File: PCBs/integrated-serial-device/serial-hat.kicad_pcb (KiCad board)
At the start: 2 copper layers, 193 x 113 mm, 30 parts, among them CN1 Modem port, CN2 Modem out 3, CN3 Printer port, J1 Rpi headers, J3 Conn_01x02_Pin, K1 Quicktake, K2 ImageWriter, SW1 Modem To Proxy, SW2 Modem to Quicktake, SW3 Modem out 3, SW5 Printer to Proxy, SW6 Printer to ImageWriter, SW7 SW_SPST, SW8 SW_Slide_DPDT SHOU HAN MSK-22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, U1 MAX3232, U2 PC817C-S

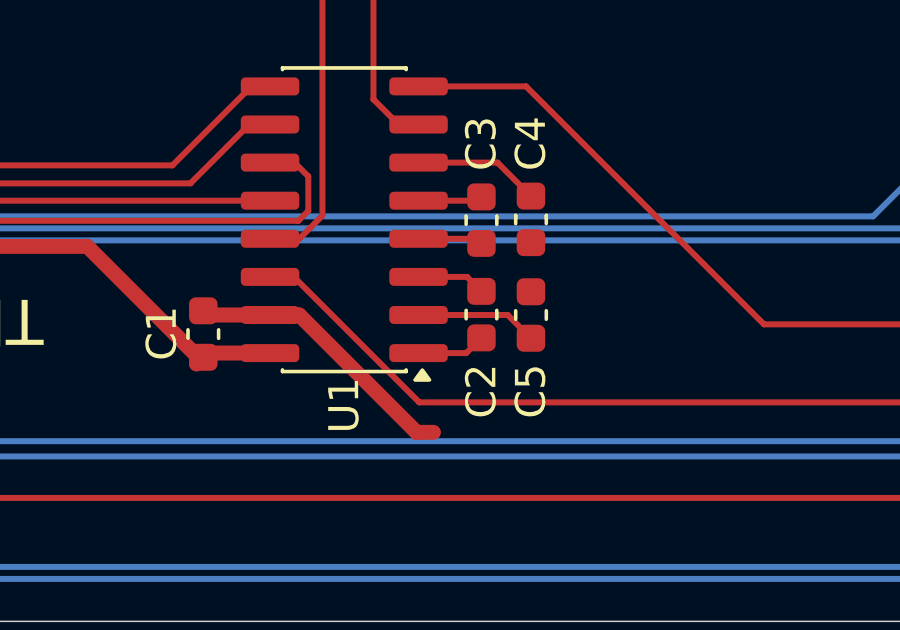
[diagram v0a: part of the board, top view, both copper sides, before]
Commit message: Add teardrops
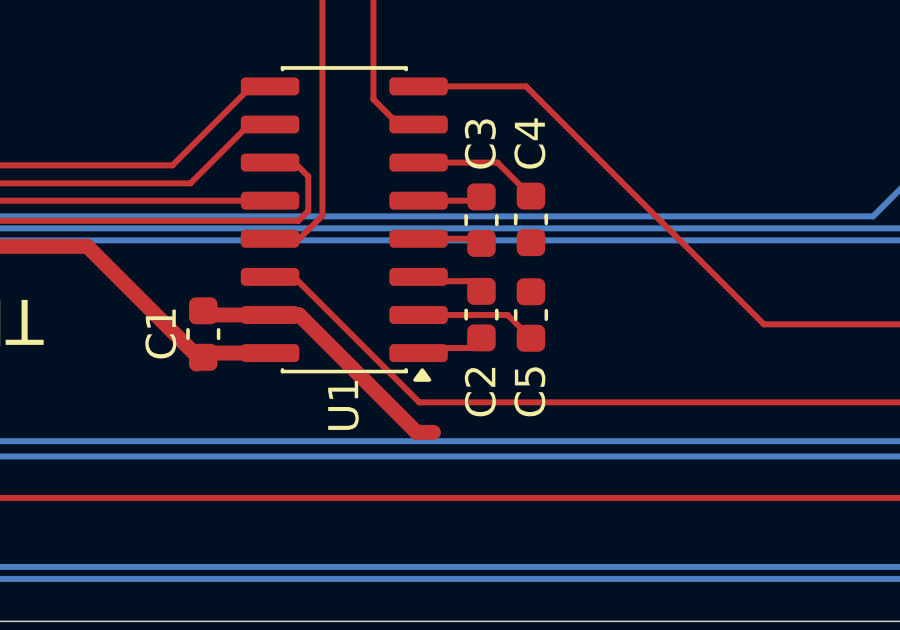
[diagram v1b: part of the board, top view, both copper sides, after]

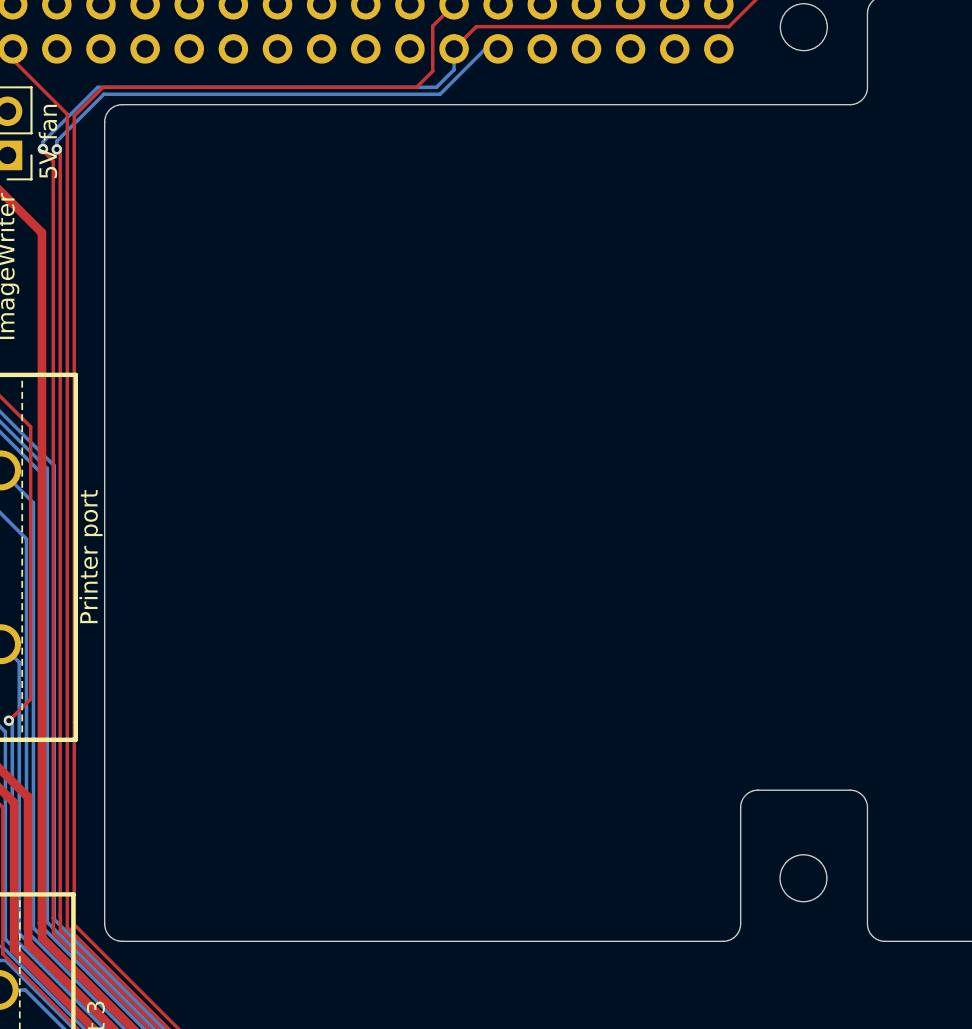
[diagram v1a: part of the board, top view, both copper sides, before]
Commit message: Add fan mounting holes
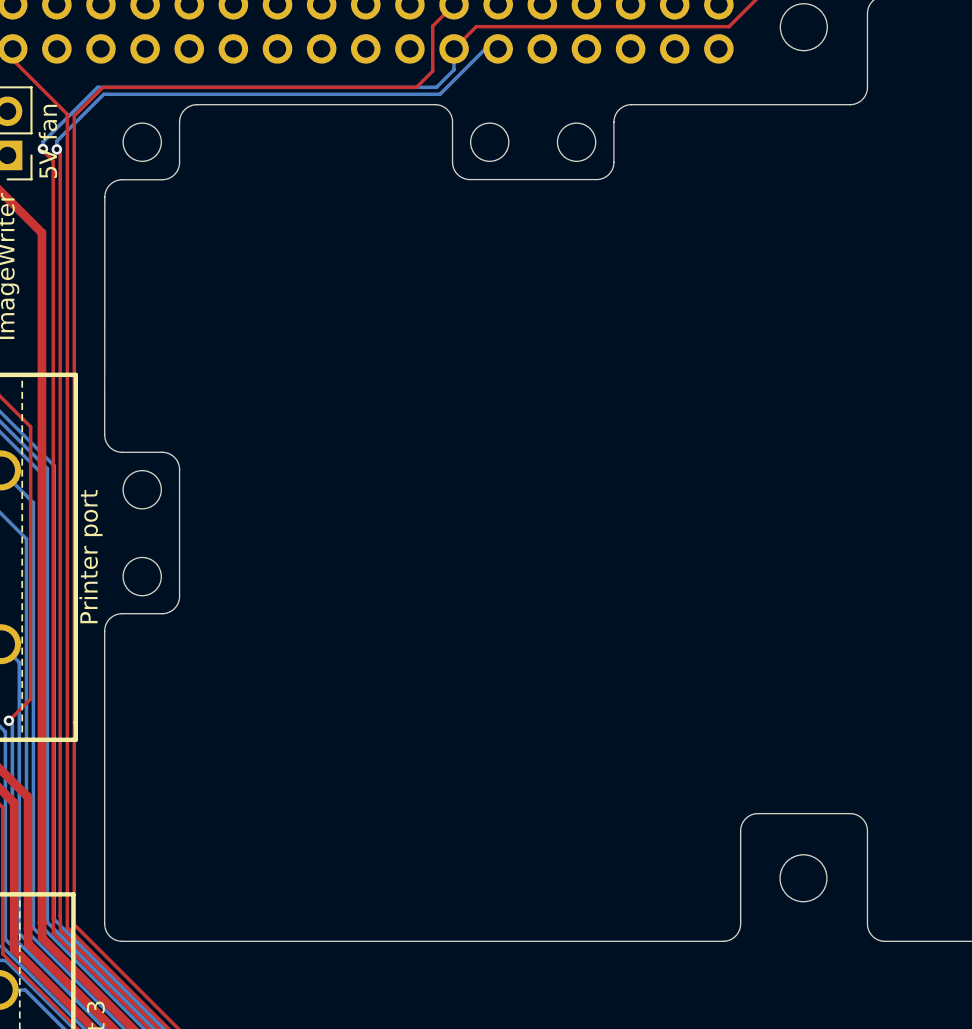
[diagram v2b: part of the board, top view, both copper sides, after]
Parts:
- added ?: , , F.Cu at (76.7, 73.6)
- added ?: , , F.Cu at (76.7, 68.6)
- added REF**: MountingHole_2.2mm_M2_DIN965, MountingHole:MountingHole_2.2mm_M2_DIN965, F.Cu at (76.7, 48.6)
- added REF**: MountingHole_2.2mm_M2_DIN965, MountingHole:MountingHole_2.2mm_M2_DIN965, F.Cu at (101.7, 48.6)
- added REF**: MountingHole_2.2mm_M2_DIN965, MountingHole:MountingHole_2.2mm_M2_DIN965, F.Cu at (96.7, 48.6)
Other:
- outline, holes or cut-outs redrawn
